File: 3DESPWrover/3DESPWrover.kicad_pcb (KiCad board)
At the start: 2 copper layers, 48.3 x 48.3 mm, 22 parts, among them J1 Conn_01x05_Male, J2 Conn_01x04, J3 Conn_02x03_Odd_Even, J4 Conn_02x07_Odd_Even, SW1 SW_Push, SW2 SW_Push, U1 ESP32-S2-WROVER

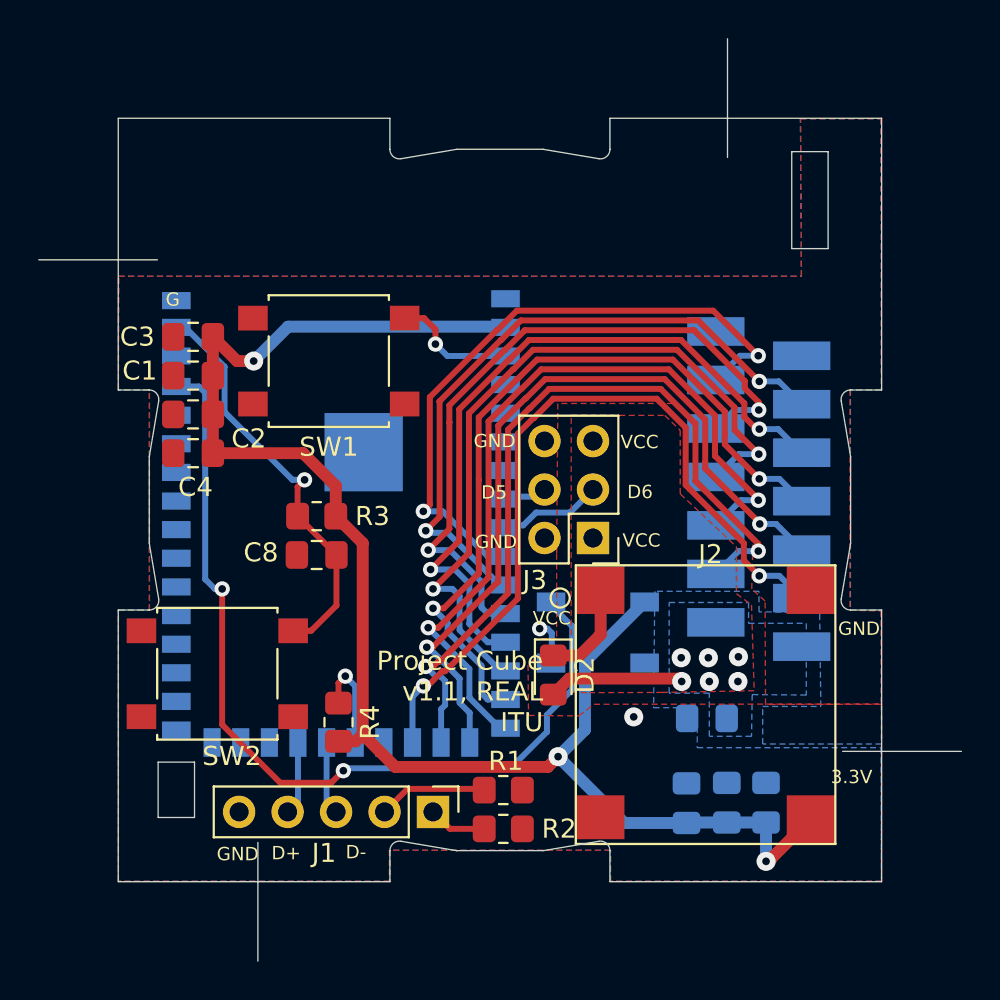
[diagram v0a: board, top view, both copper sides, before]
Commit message: Updated esp32 footprint for 9 ground path underneath and correcting misalignments
Added protection resistors to digital pins

Moved decoupling capacitors closer to 3.3v line

Corrected legend positions and added indication of boot and reset buttons
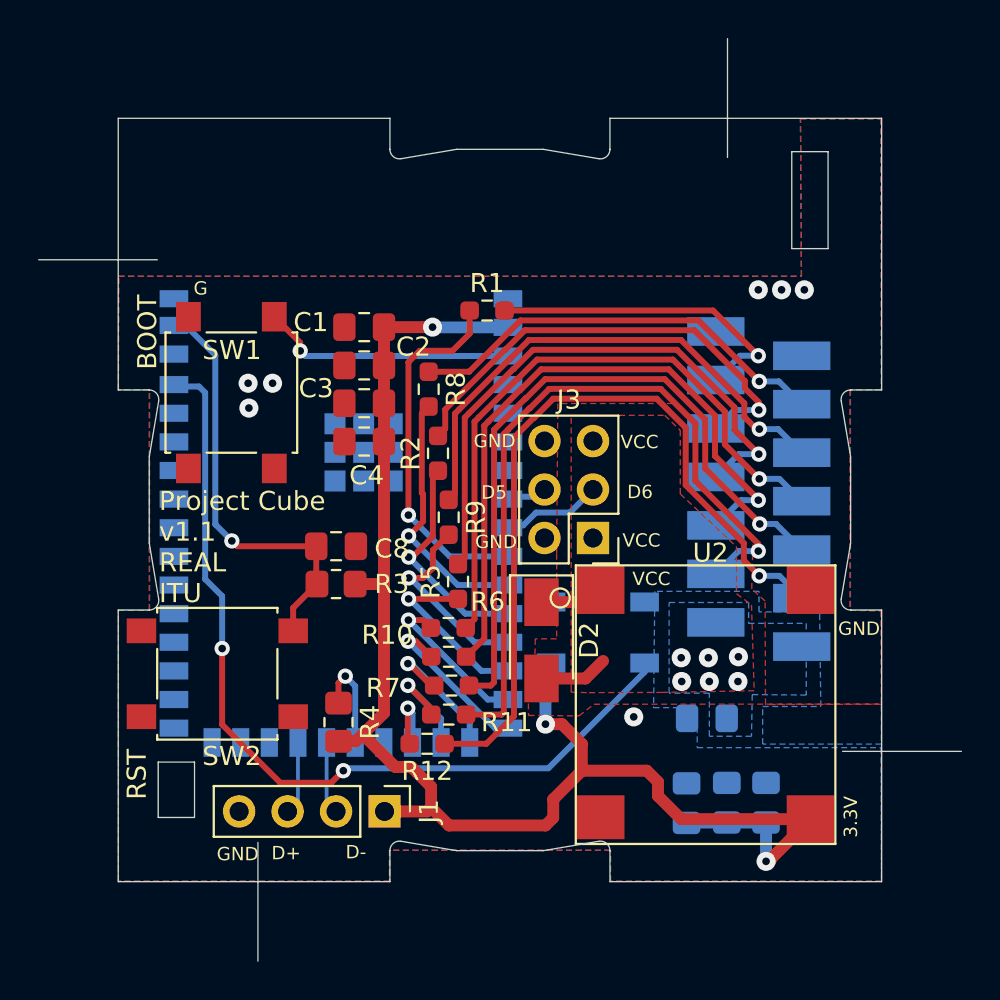
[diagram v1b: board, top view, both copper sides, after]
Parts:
- removed J2: Conn_01x04, Custom:K7803JT-500R3-SMD
- added R10: 500, Resistor_SMD:R_0603_1608Metric_Pad0.98x0.95mm_HandSolder, F.Cu at (217.2, 76.7)
- added R11: 500, Resistor_SMD:R_0603_1608Metric_Pad0.98x0.95mm_HandSolder, F.Cu at (217.4, 79.7)
- added R12: 500, Resistor_SMD:R_0603_1608Metric_Pad0.98x0.95mm_HandSolder, F.Cu at (216.1, 82.8)
- added R5: 500, Resistor_SMD:R_0603_1608Metric_Pad0.98x0.95mm_HandSolder, F.Cu at (217.7, 74.3)
- added R6: 500, Resistor_SMD:R_0603_1608Metric_Pad0.98x0.95mm_HandSolder, F.Cu at (217.2, 78.2)
- added R7: 500, Resistor_SMD:R_0603_1608Metric_Pad0.98x0.95mm_HandSolder, F.Cu at (217.2, 81.3)
- added R8: 500, Resistor_SMD:R_0603_1608Metric_Pad0.98x0.95mm_HandSolder, F.Cu at (216.2, 64.2)
- added R9: 500, Resistor_SMD:R_0603_1608Metric_Pad0.98x0.95mm_HandSolder, F.Cu at (217.2, 70.9)
- added U2: K78xxJT-500R3, Custom:K7803JT-500R3-SMD, F.Cu at (230.7, 80.7)
- D2: value D -> D_Schottky; footprint Diode_SMD:D_0805_2012Metric_Pad1.15x1.40mm_HandSolder -> Diode_SMD:D_SMA
- J1: value Conn_01x05_Male -> Conn_01x04_Male; footprint Connector_PinHeader_2.54mm:PinHeader_1x05_P2.54mm_Vertical -> Connector_PinHeader_2.54mm:PinHeader_1x04_P2.54mm_Vertical
- R1, R2: value 5.1k -> 500; footprint Resistor_SMD:R_0805_2012Metric_Pad1.20x1.40mm_HandSolder -> Resistor_SMD:R_0603_1608Metric_Pad0.98x0.95mm_HandSolder
- U1: footprint RF_Module:ESP32-S2-WROVER -> Custom:ESP32-S2-WROVER
- moved R1 25.1 mm to (219.2, 60.1)
- moved R2 20.0 mm to (216.7, 67.6), turned to 90 degrees
- moved C3 9.62 mm to (212.8, 64.9)
- moved C2 9.33 mm to (212.8, 63.0)
- moved C1 9.32 mm to (212.8, 61.0)
- moved C4 8.99 mm to (212.8, 67.0)
- moved SW1 5.37 mm to (205.8, 64.4), turned to 90 degrees
- moved R3 3.70 mm to (211.3, 74.4)
- moved J1 2.54 mm to (213.9, 86.3)
- moved D2 1.92 mm to (222.1, 77.4)
- moved C8 1.11 mm to (211.3, 72.4), turned to 0 degrees
- turned D1 to 0 degrees
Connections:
- J1 pad 1: Net-(J1-Pad1) -> +3V3
- J1 pad 2: Net-(J1-Pad2) -> /D-
- J1 pad 3: /D- -> /D+
- J1 pad 4: /D+ -> GND
- J4 pad 10: /D14 -> Net-(J4-Pad10)
- J4 pad 11: /D15 -> Net-(J4-Pad11)
- J4 pad 12: /D16 -> Net-(J4-Pad12)
- J4 pad 3: /D7 -> Net-(J4-Pad3)
- J4 pad 4: /D8 -> Net-(J4-Pad4)
- J4 pad 5: /D9 -> Net-(J4-Pad5)
- J4 pad 6: /D10 -> Net-(J4-Pad6)
- J4 pad 7: /D11 -> Net-(J4-Pad7)
- J4 pad 8: /D12 -> Net-(J4-Pad8)
- J4 pad 9: /D13 -> Net-(J4-Pad9)
- R1 pad 1: Net-(J1-Pad2) -> /D7
- R1 pad 2: GND -> Net-(J4-Pad3)
- R2 pad 1: Net-(J1-Pad1) -> /D9
- R2 pad 2: GND -> Net-(J4-Pad5)
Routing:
- net Net-(J4-Pad12): track 0.00 -> 41.4 mm, vias 0 -> 1
- net Net-(J4-Pad11): track 0.00 -> 39.2 mm, vias 0 -> 1
- net /D16: track 40.9 -> 3.81 mm, vias 2 -> 1
- net Net-(J4-Pad10): track 0.00 -> 37.1 mm, vias 0 -> 1
- net /D15: track 41.5 -> 5.75 mm, vias 2 -> 1
- net Net-(J4-Pad9): track 0.00 -> 35.0 mm, vias 0 -> 1
- net /D14: track 41.7 -> 7.27 mm, vias 2 -> 1
- net Net-(J4-Pad8): track 0.00 -> 33.6 mm, vias 0 -> 1
- net /D13: track 41.7 -> 8.67 mm, vias 2 -> 1
- net /D12: track 40.5 -> 8.28 mm, vias 2 -> 1
- net Net-(J4-Pad7): track 0.00 -> 30.4 mm, vias 0 -> 1
- net /D11: track 38.9 -> 9.36 mm, vias 2 -> 1
- net /D10: track 38.1 -> 10.1 mm, vias 2 -> 1
- net Net-(J4-Pad6): track 0.00 -> 27.3 mm, vias 0 -> 1
- net /D9: track 37.0 -> 11.7 mm, vias 2 -> 1
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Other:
- board text added: "BOOT"
- board text added: "Project Cube v1.1 REAL ITU"
- board text added: "RST"
- board text removed: "Project Cube v1.1, REAL ITU"

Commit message: Designed Pressure sensors PCB
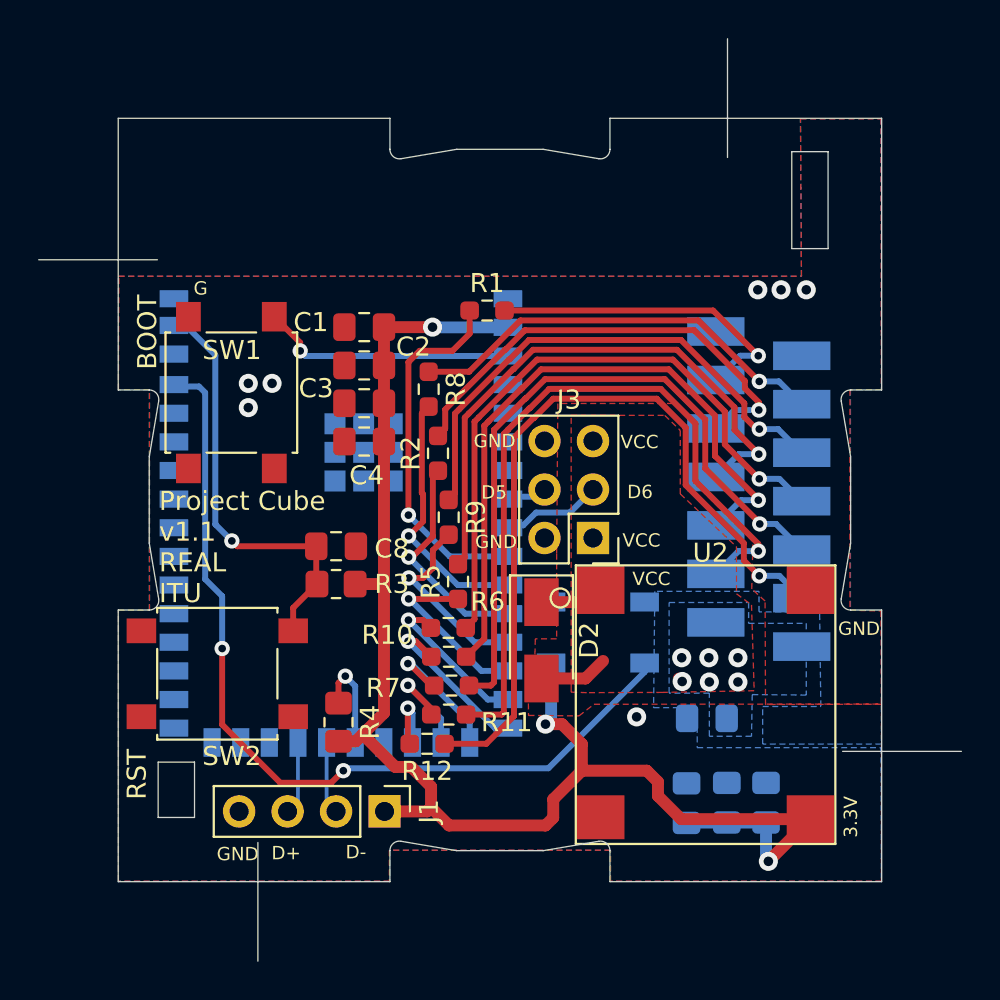
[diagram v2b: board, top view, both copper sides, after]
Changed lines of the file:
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@@
   (segment (start 233.9792 88.9508) (end 236.19 86.74) (width 0.625) (layer "F.Cu") (net 1))
   (segment (start 211.455 82.661) (end 212.36 82.661) (width 0.625) (layer "F.Cu") (net 1))
-  (segment (start 233.8578 88.9508) (end 234.0892 88.9508) (width 0.625) (layer "F.Cu") (net 1))
   (segment (start 228.1936 85.5218) (end 228.1936 84.7852) (width 0.625) (layer "F.Cu") (net 1))
   (segment (start 212.725 82.296) (end 213.8387 81.1823) (width 0.625) (layer "F.Cu") (net 1))
@@
   (segment (start 222.3008 87.0712) (end 217.2462 87.0712) (width 0.625) (layer "F.Cu") (net 1))
   (segment (start 213.8387 81.1823) (end 213.8387 74.3497) (width 0.625) (layer "F.Cu") (net 1))
-  (segment (start 233.8578 88.9508) (end 233.9692 88.9508) (width 0.625) (layer "F.Cu") (net 1))
   (segment (start 213.8387 60.96) (end 213.8387 62.9666) (width 0.625) (layer "F.Cu") (net 1))
   (segment (start 222.7072 85.698778) (end 222.7072 86.6648) (width 0.625) (layer "F.Cu") (net 1))
   (segment (start 215.27169 84.00449) (end 214.43349 84.00449) (width 0.625) (layer "F.Cu") (net 1))
   (segment (start 216.3826 60.96) (end 213.8387 60.96) (width 0.625) (layer "F.Cu") (net 1))
-  (segment (start 233.8578 88.9508) (end 233.9792 88.9508) (width 0.625) (layer "F.Cu") (net 1))
   (segment (start 213.7664 74.422) (end 213.8387 74.3497) (width 0.625) (layer "F.Cu") (net 1))
   (segment (start 213.868 86.3346) (end 216.1032 86.3346) (width 0.625) (layer "F.Cu") (net 1))
@@
   (segment (start 214.43349 84.00449) (end 212.725 82.296) (width 0.625) (layer "F.Cu") (net 1))
   (segment (start 216.3064 86.1314) (end 216.3064 85.0392) (width 0.625) (layer "F.Cu") (net 1))
-  (via (at 216.3826 60.96) (size 1) (drill 0.4) (layers "F.Cu" "B.Cu") (net 1))
-  (via (at 233.8578 88.9508) (size 1) (drill 0.4) (layers "F.Cu" "B.Cu") (net 1))
-  (via (at 222.3008 81.7626) (size 1) (drill 0.4) (layers "F.Cu" "B.Cu") (net 1))
-  (segment (start 222.3008 81.7626) (end 222.3008 78.8552) (width 0.625) (layer "B.Cu") (net 1))
-  (segment (start 222.3008 78.8552) (end 222.594 78.562) (width 0.625) (layer "B.Cu") (net 1))
+  (via (at 216.3826 60.96) (size 1) (drill 0.5) (layers "F.Cu" "B.Cu") (net 1))
+  (via (at 222.3008 81.7626) (size 1) (drill 0.5) (layers "F.Cu" "B.Cu") (net 1))
+  (via (at 233.9792 88.9508) (size 1) (drill 0.5) (layers "F.Cu" "B.Cu") (net 1))
+  (segment (start 233.8578 86.9149) (end 231.8004 86.9149) (width 0.625) (layer "B.Cu") (net 1))
+  (segment (start 233.8578 86.9149) (end 233.8578 88.8294) (width 0.625) (layer "B.Cu") (net 1))
+  (segment (start 222.594 81.4694) (end 222.3008 81.7626) (width 0.625) (layer "B.Cu") (net 1))
+  (segment (start 229.7176 86.9149) (end 229.6922 86.9403) (width 0.625) (layer "B.Cu") (net 1))
+  (segment (start 222.594 78.562) (end 222.594 81.4694) (width 0.625) (layer "B.Cu") (net 1))
+  (segment (start 220.332 60.972) (end 216.3946 60.972) (width 0.625) (layer "B.Cu") (net 1))
+  (segment (start 220.092 60.96) (end 220.207 60.845) (width 0.625) (layer "B.Cu") (net 1))
+  (segment (start 233.8578 88.8294) (end 233.9792 88.9508) (width 0.625) (layer "B.Cu") (net 1))
   (segment (start 216.3946 60.972) (end 216.3826 60.96) (width 0.625) (layer "B.Cu") (net 1))
-  (segment (start 233.8578 86.9149) (end 231.8004 86.9149) (width 0.625) (layer "B.Cu") (net 1))
-  (segment (start 229.7176 86.9149) (end 229.6922 86.9403) (width 0.625) (layer "B.Cu") (net 1))
-  (segment (start 220.092 60.96) (end 220.207 60.845) (width 0.625) (layer "B.Cu") (net 1))
-  (segment (start 233.8578 88.9508) (end 233.8578 86.9149) (width 0.625) (layer "B.Cu") (net 1))
-  (segment (start 220.332 60.972) (end 216.3946 60.972) (width 0.625) (layer "B.Cu") (net 1))
   (segment (start 220.207 60.972) (end 220.171499 60.936499) (width 0.625) (layer "B.Cu") (net 1))
   (segment (start 231.8004 86.9149) (end 229.7176 86.9149) (width 0.625) (layer "B.Cu") (net 1))
-  (via (at 226.9236 81.3816) (size 1) (drill 0.4) (layers "F.Cu" "B.Cu") (net 2))
-  (via (at 206.76 65.2) (size 1) (drill 0.4) (layers "F.Cu" "B.Cu") (net 2))
-  (via (at 233.4514 59.0042) (size 1) (drill 0.4) (layers "F.Cu" "B.Cu") (net 2))
-  (via (at 206.72 63.9) (size 1) (drill 0.4) (layers "F.Cu" "B.Cu") (net 2))
-  (via (at 234.6706 59.0042) (size 1) (drill 0.4) (layers "F.Cu" "B.Cu") (net 2))
-  (via (at 208 63.9) (size 1) (drill 0.4) (layers "F.Cu" "B.Cu") (net 2))
-  (via (at 235.8644 59.0042) (size 1) (drill 0.4) (layers "F.Cu" "B.Cu") (net 2))
+  (via (at 234.6452 59.0042) (size 1) (drill 0.5) (layers "F.Cu" "B.Cu") (net 2))
+  (via (at 227.076 81.3816) (size 1) (drill 0.5) (layers "F.Cu" "B.Cu") (net 2))
+  (via (at 233.426 59.0042) (size 1) (drill 0.5) (layers "F.Cu" "B.Cu") (net 2))
+  (via (at 207.9752 63.9064) (size 1) (drill 0.5) (layers "F.Cu" "B.Cu") (net 2))
+  (via (at 206.7306 63.9064) (size 1) (drill 0.5) (layers "F.Cu" "B.Cu") (net 2))
+  (via (at 235.966 59.0042) (size 1) (drill 0.5) (layers "F.Cu" "B.Cu") (net 2))
+  (via (at 206.7306 65.1764) (size 1) (drill 0.5) (layers "F.Cu" "B.Cu") (net 2))
   (segment (start 222.09 79.37) (end 224.4 79.37) (width 0.625) (layer "F.Cu") (net 3))
   (segment (start 224.4 79.37) (end 225.32 78.45) (width 0.625) (layer "F.Cu") (net 3))
   (segment (start 229.2858 79.375) (end 229.4382 79.5274) (width 0.625) (layer "F.Cu") (net 3))
-  (via (at 230.8352 78.2828) (size 1) (drill 0.4) (layers "F.Cu" "B.Cu") (net 3))
-  (via (at 229.4128 78.2828) (size 1) (drill 0.4) (layers "F.Cu" "B.Cu") (net 3))
-  (via (at 232.41 78.232) (size 1) (drill 0.4) (layers "F.Cu" "B.Cu") (net 3))
-  (via (at 232.3846 79.5274) (size 1) (drill 0.4) (layers "F.Cu" "B.Cu") (net 3))
-  (via (at 229.4382 79.5274) (size 1) (drill 0.4) (layers "F.Cu" "B.Cu") (net 3))
-  (via (at 230.886 79.5274) (size 1) (drill 0.4) (layers "F.Cu" "B.Cu") (net 3))
+  (via (at 232.3846 78.2828) (size 1) (drill 0.5) (layers "F.Cu" "B.Cu") (net 3))
+  (via (at 230.8606 78.2828) (size 1) (drill 0.5) (layers "F.Cu" "B.Cu") (net 3))
+  (via (at 229.4636 79.5274) (size 1) (drill 0.5) (layers "F.Cu" "B.Cu") (net 3))
+  (via (at 229.4382 78.2828) (size 1) (drill 0.5) (layers "F.Cu" "B.Cu") (net 3))
+  (via (at 230.886 79.5528) (size 1) (drill 0.5) (layers "F.Cu" "B.Cu") (net 3))
+  (via (at 232.3846 79.5528) (size 1) (drill 0.5) (layers "F.Cu" "B.Cu") (net 3))
   (segment (start 209.08 76.871) (end 209.08 75.67) (width 0.3125) (layer "F.Cu") (net 4))
   (segment (start 209.08 75.67) (end 210.328 74.422) (width 0.3125) (layer "F.Cu") (net 4))
